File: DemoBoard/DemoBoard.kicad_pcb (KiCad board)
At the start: 2 copper layers, 45 x 45 mm, 58 parts, among them J1 USB4110GFA, J2 Conn_01x10_Pin, J3 Conn_01x10_Pin, J4 Conn_01x10_Pin, J5 Conn_01x10_Pin, SW1 SW_Push, SW2 SW_Push, U1 RP2040, U2 W25Q128JVSIM, U3 MCP2518FDT-E_QBB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

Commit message: Routing, Placement, and BOM
See above
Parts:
- removed J2, J3, J4, J5: Conn_01x10_Pin, Connector_PinSocket_2.54mm:PinSocket_1x10_P2.54mm_Vertical
- removed JP1: 3, Jumper:SolderJumper-2_P1.3mm_Open_RoundedPad1.0x1.5mm
- removed JP2: 2, Jumper:SolderJumper-2_P1.3mm_Open_RoundedPad1.0x1.5mm
- removed JP3: 1, Jumper:SolderJumper-2_P1.3mm_Open_RoundedPad1.0x1.5mm
- removed JP4: 0, Jumper:SolderJumper-2_P1.3mm_Open_RoundedPad1.0x1.5mm
- added C24: 100nF, Capacitor_SMD:C_0402_1005Metric_Pad0.74x0.62mm_HandSolder, F.Cu at (143.6, 64.2)
- added C25: 47uF, Capacitor_SMD:C_1206_3216Metric_Pad1.33x1.80mm_HandSolder, F.Cu at (144.6, 45.6)
- added J6: M55-7101242R, inspireFly:HARWIN_M55-7101242R, F.Cu at (139.3, 39.8)
- added J7: MSD-1-A, inspireFly:CUI_MSD-1-A, F.Cu at (154.3, 63.2)
- added J8: Conn_01x17_Pin, Connector_PinSocket_2.54mm:PinSocket_1x17_P2.54mm_Vertical, F.Cu at (119.1, 75.9)
- added R11: 10k, Resistor_SMD:R_0402_1005Metric_Pad0.72x0.64mm_HandSolder, F.Cu at (143.6, 62.9)
- C22: footprint Capacitor_SMD:C_0402_1005Metric -> Capacitor_SMD:C_0402_1005Metric_Pad0.74x0.62mm_HandSolder
- C23: value 10uF -> 47uF; footprint Capacitor_SMD:C_0402_1005Metric -> Capacitor_SMD:C_1206_3216Metric_Pad1.33x1.80mm_HandSolder
- D1, D2, R8, R9: moved to B.Cu
- JP5: value SolderJumper_2_Open -> 3.3V EN; footprint Jumper:SolderJumper-2_P1.3mm_Open_RoundedPad1.0x1.5mm -> inspireFly:SmallJumper
- moved Y2 45.3 mm to (121.0, 43.6), turned to 180 degrees
- moved U4 42.0 mm to (127.2, 36.1)
- moved D2 40.7 mm to (123.2, 71.6)
- moved D1 40.3 mm to (123.3, 68.4)
- moved TP3 38.0 mm to (151.3, 37.1)
- moved TP2 36.8 mm to (154.4, 37.1)
- moved SW2 36.3 mm to (119.6, 52.3), turned to 90 degrees
- moved J1 34.7 mm to (155.2, 47.1), turned to 90 degrees
- moved R10 34.5 mm to (130.9, 36.4), turned to -90 degrees
- moved SW1 33.6 mm to (119.6, 59.4), turned to 90 degrees
- moved C22 33.1 mm to (148.9, 37.3), turned to 90 degrees
- moved R6 33.0 mm to (156.2, 39.9), turned to 180 degrees
- moved R7 29.9 mm to (120.2, 48.4), turned to 180 degrees
- moved U2 27.8 mm to (128.4, 51.2), turned to 45 degrees
- moved C2 27.0 mm to (136.1, 66.2)
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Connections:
- net SPI0_CS renamed SPI0_CS_CAN
- R8 pad 1: GPIO_5_DEBUGLED -> GPIO_6
- U1 pad 7: GPIO_5_DEBUGLED -> SPI0_CS_SDCARD
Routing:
- net CAN_LOW: track 0.00 -> 61.7 mm, vias 0 -> 3
- net CAN_HIGH: track 0.00 -> 61.4 mm, vias 0 -> 1
- net USB_VOLTAGE: track 0.00 -> 53.2 mm, vias 0 -> 1
- net +3.3V: track 0.00 -> 49.6 mm, vias 0 -> 20
- net GPIO_15: track 0.00 -> 42.9 mm, vias 0 -> 2
- net GPIO_14: track 0.00 -> 41.9 mm, vias 0 -> 2
- net SPI0_MOSI: track 0.00 -> 38.6 mm, vias 0 -> 4
- net SPI0_MISO: track 0.00 -> 38.2 mm, vias 0 -> 3
- net GPIO_9: track 0.00 -> 35.6 mm
- net ADC_3: track 0.00 -> 35.5 mm, vias 0 -> 1
- net SPI0_CLK: track 0.00 -> 34.7 mm, vias 0 -> 4
- net ADC_2: track 0.00 -> 34.0 mm, vias 0 -> 1
- net ADC_0: track 0.00 -> 33.8 mm, vias 0 -> 1
- net ADC_1: track 0.00 -> 33.5 mm, vias 0 -> 1
- net GPIO_17: track 0.00 -> 26.8 mm, vias 0 -> 2
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- added copper zone on F.Cu, net +3.3V
- added copper zone on In2.Cu, net +3.3V
- added copper zone on F.Cu, net BATTERY_VOLTAGE
- added copper zone on B.Cu, net GND
- added copper zone on F.Cu, net GND
- added copper zone on In1.Cu, net GND
- added copper zone on F.Cu, net USB_VOLTAGE
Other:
- copper layers 2 -> 4
- board text added: "BOOT0"
- board text added: "CAN L CAN H +3.3V SWCLK GND SWD USB_V A0 A1 A2 A3 9 14 15 16 17 GND"
- board text added: "RST"

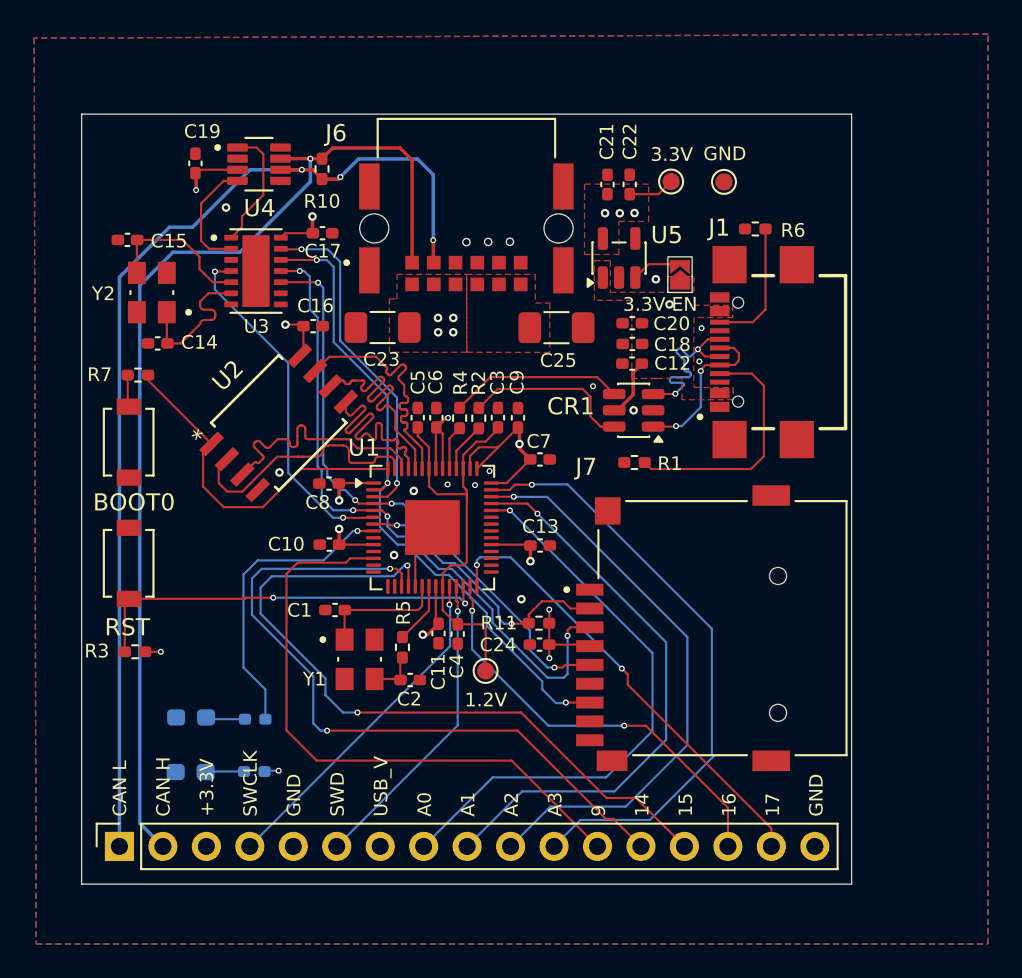
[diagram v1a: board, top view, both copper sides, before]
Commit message: Final Board Order Changes
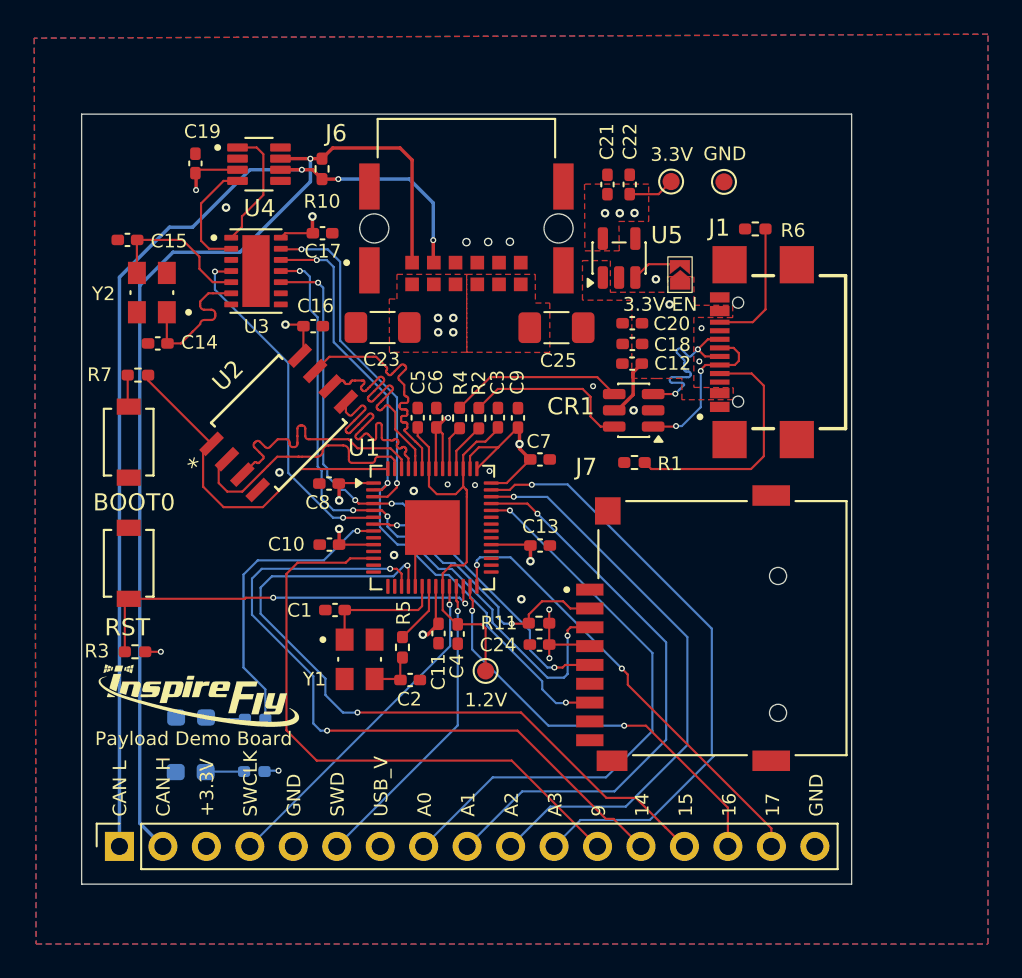
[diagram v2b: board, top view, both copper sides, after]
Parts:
- added G***: LOGO, inspireFly:longInspireFly_12mmX4mm, F.Cu at (123.7, 67.1)
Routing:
- net CAN_LOW: track 61.7 -> 59.8 mm
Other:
- board text added: "Payload Demo Board"

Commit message: Updated DemoBoard to V0.2
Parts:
- removed U3: MCP2518FDT-E_QBB, inspireFly:SON65P450X300X90-15N
- added R12: 10k, Resistor_SMD:R_0402_1005Metric_Pad0.72x0.64mm_HandSolder, F.Cu at (130.5, 43.6)
- added U6: MCP2515T-I/ML, inspireFly:QFN20_4x4MC_MCH, F.Cu at (126.2, 42.5)
- C14, C15: value 18pF -> 15pF
- moved C17 1.37 mm to (130.5, 41.4)
- moved C15 0.22 mm to (119.5, 40.7)
- moved Y2 0.09 mm to (121.0, 43.7)
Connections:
- U1 pad 13: GPIO_10 -> SPI1_CLK
- U1 pad 14: GPIO_11 -> SPI1_MOSI
- U1 pad 15: GPIO_12 -> SPI1-MISO
- U1 pad 16: GPIO_13 -> SPI1_CS_CAN
- U1 pad 3: SPI0_CS_CAN -> GPIO_1
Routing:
- net SPI1_CS_CAN: track 0.00 -> 27.2 mm, vias 0 -> 2
- net SPI1-MISO: track 0.00 -> 24.0 mm, vias 0 -> 2
- net SPI0_CS_CAN: track 19.9 -> 0.00 mm, vias 2 -> 0
- net SPI1_MOSI: track 0.00 -> 19.8 mm, vias 0 -> 2
- net SPI1_CLK: track 0.00 -> 19.5 mm, vias 0 -> 2
- net SPI0_MOSI: track 38.6 -> 20.2 mm, vias 4 -> 2
- net SPI0_MISO: track 38.2 -> 21.0 mm, vias 3 -> 2
- net SPI0_CLK: track 34.7 -> 17.6 mm, vias 4 -> 2
- net GPIO_15: track 42.9 -> 34.9 mm
- net INT_CAN_CONTROLLER: track 20.6 -> 16.5 mm
- net Net-(U6-*RESET): track 0.00 -> 4.05 mm
- net +3.3V: track 49.6 -> 52.1 mm
- net Net-(U6-OSC1): track 8.86 -> 6.63 mm
- net Net-(U6-OSC2): track 8.87 -> 6.66 mm
- net GPIO_6: track 17.8 -> 19.9 mm
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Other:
- board text added: "Payload Demo Board V2"
- board text removed: "Payload Demo Board"

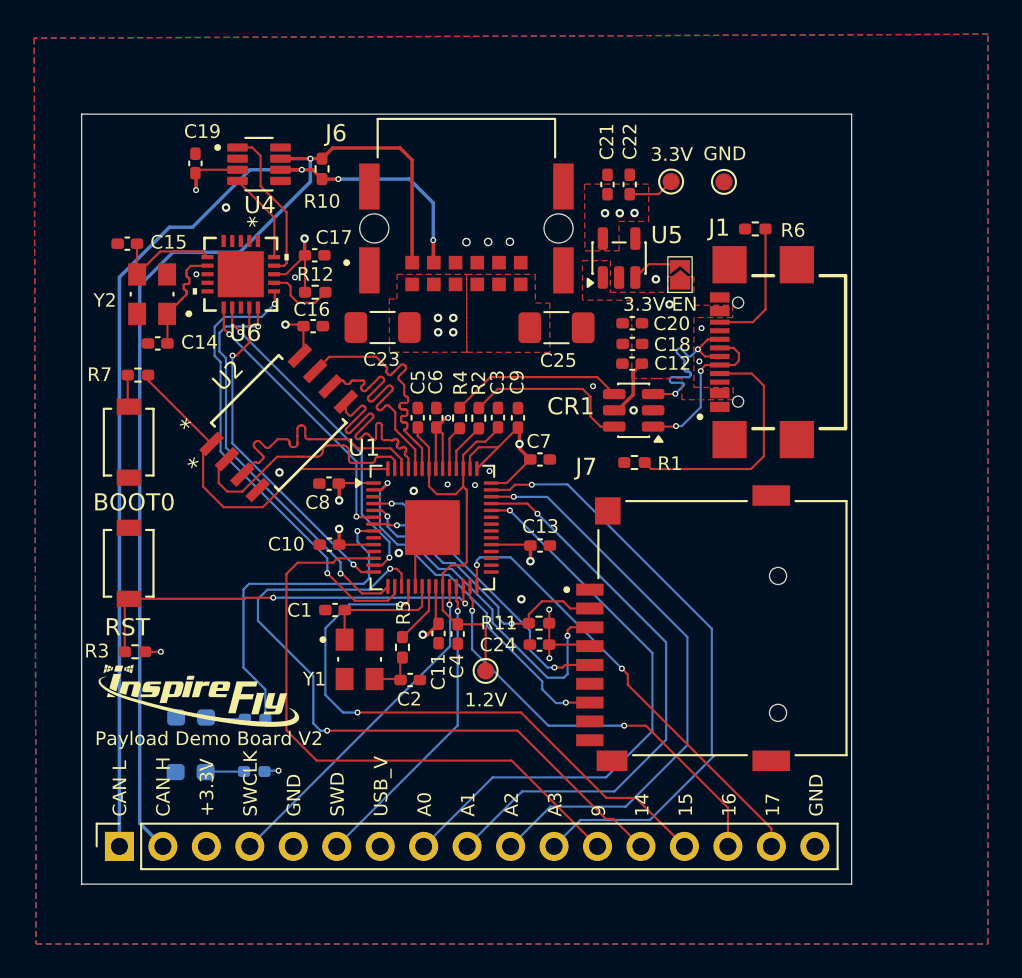
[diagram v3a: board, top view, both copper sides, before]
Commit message: Fix silkscreen on Demoboard
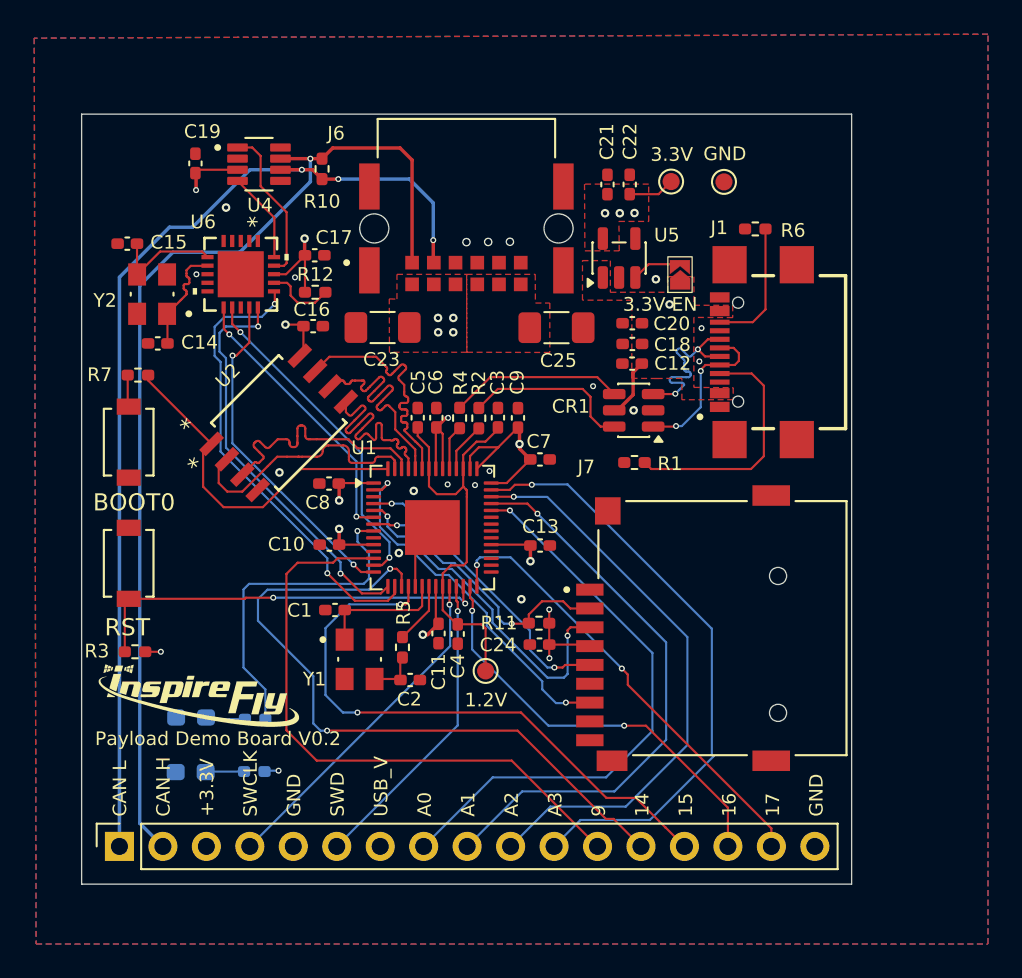
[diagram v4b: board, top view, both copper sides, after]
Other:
- board text added: "Payload Demo Board V0.2"
- board text removed: "Payload Demo Board V2"
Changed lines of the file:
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@@
 		(tags "capacitor handsolder")
 		(property "Reference" "C11"
-			(at -2.24 -0.01 90)
+			(at -2.24 0.0025 90)
 			(layer "F.SilkS")
 			(effects
@@
 			(effects
 				(font
-					(size 1 1)
-					(thickness 0.15)
+					(size 0.8 0.8)
+					(thickness 0.1)
 				)
 			)
@@
 			(effects
 				(font
-					(size 1 1)
-					(thickness 0.15)
+					(size 0.8 0.8)
+					(thickness 0.1)
 				)
 			)
@@
 			(effects
 				(font
-					(size 1 1)
-					(thickness 0.15)
+					(size 0.8 0.8)
+					(thickness 0.1)
 				)
 			)
@@
 			(effects
 				(font
-					(size 1 1)
-					(thickness 0.15)
+					(size 0.8 0.8)
+					(thickness 0.1)
 				)
 			)
@@
 			(effects
 				(font
-					(size 1 1)
-					(thickness 0.15)
+					(size 0.8 0.8)
+					(thickness 0.1)
 				)
 			)
@@
 		(tags "capacitor handsolder")
 		(property "Reference" "C4"
-			(at 1.88 0.05 90)
+			(at 1.8775 -0.0025 90)
 			(layer "F.SilkS")
 			(effects
@@
 			(effects
 				(font
-					(size 1 1)
-					(thickness 0.15)
+					(size 0.8 0.8)
+					(thickness 0.1)
 				)
 			)
@@
 			(effects
 				(font
-					(size 1 1)
-					(thickness 0.15)
+					(size 0.8 0.8)
+					(thickness 0.1)
 				)
 			)
@@
 			(effects
 				(font
-					(size 1 1)
-					(thickness 0.15)
+					(size 0.8 0.8)
+					(thickness 0.1)
 				)
 			)
@@
 			(effects
 				(font
-					(size 1 1)
-					(thickness 0.15)
+					(size 0.8 0.8)
+					(thickness 0.1)
 				)
 			)
@@
 			(effects
 				(font
-					(size 1 1)
-					(thickness 0.15)
+					(size 0.8 0.8)
+					(thickness 0.1)
 				)
 			)
@@
 		(tags "MCP2515T-I/ML ")
 		(property "Reference" "U6"
-			(at 3.4331 -0.269999 0)
+			(at -3.0569 2.200001 0)
 			(unlocked yes)
 			(layer "F.SilkS")
 			(effects
 				(font
-					(size 1 1)
-					(thickness 0.15)
+					(size 0.8 0.8)
+					(thickness 0.1)
 				)
 			)
@@
 				(font
 					(size 0.8 0.8)
+					(thickness 0.1)
 				)
 			)
@@
 			(effects
 				(font
-					(size 1 1)
-					(thickness 0.15)
+					(size 0.8 0.8)
+					(thickness 0.1)
 				)
 			)
@@
 			(effects
 				(font
-					(size 0.787402 0.787402)
-					(thickness 0.15)
+					(size 0.8 0.8)
+					(thickness 0.1)
 				)
 			)
@@
 			(effects
 				(font
-					(size 1 1)
-					(thickness 0.15)
+					(size 0.8 0.8)
+					(thickness 0.1)
 				)
 			)
@@
 			(effects
 				(font
-					(size 1.5 1.5)
-					(thickness 0.3)
+					(size 0.8 0.8)
+					(thickness 0.1)
 				)
 			)
@@
 			(effects
 				(font
-					(size 1 1)
-					(thickness 0.15)
+					(size 0.8 0.8)
+					(thickness 0.1)
 				)
 			)
@@
 		)
 	)
-	(gr_text "Payload Demo Board V2"
+	(gr_text "Payload Demo Board V0.2"
 		(at 117.64 70.12 0)
 		(layer "F.SilkS")
